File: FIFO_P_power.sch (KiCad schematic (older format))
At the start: 19 parts, among them J4 Jack-DC, U11 LM2940CT-5.0, U12 UA79M05CKCS_-5V, U13 LM2940CT-3.3

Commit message: Fix arduino header, started laying out connectors
The pins used were changed, so the old code must be rewritten to use the new pins and port D instead of port A.
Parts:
- renumbered J4 to J5, TP5 to TP4, TP6 to TP5, TP7 to TP6, TP8 to TP7, TP9 to TP8
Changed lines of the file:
@@
 $EndComp
 $Comp
-L power:GND #PWR036
+L power:GND #PWR038
 U 1 1 5C531288
 P 2950 1400
-F 0 "#PWR036" H 2950 1150 50  0001 C CNN
+F 0 "#PWR038" H 2950 1150 50  0001 C CNN
 F 1 "GND" H 2950 1250 50  0000 C CNN
 F 2 "" H 2950 1400 50  0000 C CNN
@@
 	2800 2350 2800 2600
 $Comp
-L power:GND #PWR035
+L power:GND #PWR037
 U 1 1 5C5322F0
 P 1800 2050
-F 0 "#PWR035" H 1800 1800 50  0001 C CNN
+F 0 "#PWR037" H 1800 1800 50  0001 C CNN
 F 1 "GND" H 1800 1900 50  0000 C CNN
 F 2 "" H 1800 2050 50  0000 C CNN
@@
 Connection ~ 3050 850
 $Comp
-L Connector:TestPoint TP5
+L Connector:TestPoint TP4
 U 1 1 5D244D32
 P 1400 850
-F 0 "TP5" H 1458 968 50  0000 L CNN
+F 0 "TP4" H 1458 968 50  0000 L CNN
 F 1 "TestPoint" H 1458 877 50  0000 L CNN
 F 2 "FIFO_P:Test_Pin" H 1600 850 50  0001 C CNN
@@
 $EndComp
 $Comp
-L Connector:TestPoint TP7
+L Connector:TestPoint TP6
 U 1 1 5D2450B6
 P 3050 850
-F 0 "TP7" H 3108 968 50  0000 L CNN
+F 0 "TP6" H 3108 968 50  0000 L CNN
 F 1 "TestPoint" H 3108 877 50  0000 L CNN
 F 2 "FIFO_P:Test_Pin" H 3250 850 50  0001 C CNN
@@
 $EndComp
 $Comp
-L Connector:TestPoint TP9
+L Connector:TestPoint TP8
 U 1 1 5D2454BF
 P 4600 850
-F 0 "TP9" H 4658 968 50  0000 L CNN
+F 0 "TP8" H 4658 968 50  0000 L CNN
 F 1 "TestPoint" H 4658 877 50  0000 L CNN
 F 2 "FIFO_P:Test_Pin" H 4800 850 50  0001 C CNN
@@
 $EndComp
 $Comp
-L Connector:TestPoint TP8
+L Connector:TestPoint TP7
 U 1 1 5D245994
 P 3600 2050
-F 0 "TP8" H 3658 2168 50  0000 L CNN
+F 0 "TP7" H 3658 2168 50  0000 L CNN
 F 1 "TestPoint" H 3658 2077 50  0000 L CNN
 F 2 "FIFO_P:Test_Pin" H 3800 2050 50  0001 C CNN
@@
 $EndComp
 $Comp
-L Connector:TestPoint TP6
+L Connector:TestPoint TP5
 U 1 1 5D245F67
 P 2800 2700
-F 0 "TP6" H 2650 2750 50  0000 C CNN
+F 0 "TP5" H 2650 2750 50  0000 C CNN
 F 1 "TestPoint" H 2550 2850 50  0000 C CNN
 F 2 "FIFO_P:Test_Pin" H 3000 2700 50  0001 C CNN
@@
 	3050 850  3250 850
 $Comp
-L Connector:Jack-DC J4
+L Connector:Jack-DC J5
 U 1 1 5D418214
 P 700 950
-F 0 "J4" H 700 1250 50  0000 C CNN
+F 0 "J5" H 700 1250 50  0000 C CNN
 F 1 "Jack-DC" H 700 1150 50  0000 C CNN
 F 2 "Connector_BarrelJack:BarrelJack_Horizontal" H 750 910 50  0001 C CNN
@@
 $EndComp
 $Comp
-L power:GND #PWR0101
+L power:GND #PWR036
 U 1 1 5D419D2C
 P 1150 1050
-F 0 "#PWR0101" H 1150 800 50  0001 C CNN
+F 0 "#PWR036" H 1150 800 50  0001 C CNN
 F 1 "GND" H 1155 877 50  0000 C CNN
 F 2 "" H 1150 1050 50  0001 C CNN

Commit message: Most routing done
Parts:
- added C? (x4): C, symbol Device:C
- added U?: LM2776, Package_TO_SOT_SMD:SOT-23-6, symbol Regulator_SwitchedCapacitor:LM2776
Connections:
- wire segments 37 -> 47
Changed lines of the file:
@@
 Wire Wire Line
 	2800 2700 2800 2600
+$Comp
+L Device:C C?
+U 1 1 5D14A942
+P 2100 4050
+F 0 "C?" H 2215 4096 50  0000 L CNN
+F 1 "C" H 2215 4005 50  0000 L CNN
+F 2 "" H 2138 3900 50  0001 C CNN
+F 3 "~" H 2100 4050 50  0001 C CNN
+	1    2100 4050
+	1    0    0    -1
+$EndComp
+Wire Wire Line
+	2400 3900 2100 3900
+Wire Wire Line
+	2100 4200 2350 4200
+Wire Wire Line
+	2350 4200 2350 4100
+Wire Wire Line
+	2350 4100 2400 4100
+$Comp
+L power:GND #PWR?
+U 1 1 5D14C1B1
+P 2800 4300
+F 0 "#PWR?" H 2800 4050 50  0001 C CNN
+F 1 "GND" H 2805 4127 50  0000 C CNN
+F 2 "" H 2800 4300 50  0001 C CNN
+F 3 "" H 2800 4300 50  0001 C CNN
+	1    2800 4300
+	1    0    0    -1
+$EndComp
+$Comp
+L Regulator_SwitchedCapacitor:LM2776 U?
+U 1 1 5D148E12
+P 2800 3900
+F 0 "U?" H 3150 3900 50  0000 L CNN
+F 1 "LM2776" H 3150 3800 50  0000 L CNN
+F 2 "Package_TO_SOT_SMD:SOT-23-6" H 2850 3550 50  0001 L CNN
+F 3 "http://www.ti.com/lit/ds/symlink/lm2776.pdf" H 950 5150 50  0001 C CNN
+	1    2800 3900
+	1    0    0    -1
+$EndComp
+Wire Wire Line
+	2400 3800 2350 3800
+Wire Wire Line
+	2350 3800 2350 3550
+Wire Wire Line
+	2350 3550 2800 3550
+Wire Wire Line
+	2800 3550 2800 3600
+Wire Wire Line
+	3200 3800 3650 3800
+$Comp
+L Device:C C?
+U 1 1 5D150015
+P 3650 3950
+F 0 "C?" H 3765 3996 50  0000 L CNN
+F 1 "C" H 3765 3905 50  0000 L CNN
+F 2 "" H 3688 3800 50  0001 C CNN
+F 3 "~" H 3650 3950 50  0001 C CNN
+	1    3650 3950
+	1    0    0    -1
+$EndComp
+Connection ~ 3650 3800
+Wire Wire Line
+	3650 3800 4000 3800
+$Comp
+L Device:C C?
+U 1 1 5D15083E
+P 4000 3950
+F 0 "C?" H 4115 3996 50  0000 L CNN
+F 1 "C" H 4115 3905 50  0000 L CNN
+F 2 "" H 4038 3800 50  0001 C CNN
+F 3 "~" H 4000 3950 50  0001 C CNN
+	1    4000 3950
+	1    0    0    -1
+$EndComp
+$Comp
+L power:GND #PWR?
+U 1 1 5D150EB8
+P 3650 4100
+F 0 "#PWR?" H 3650 3850 50  0001 C CNN
+F 1 "GND" H 3655 3927 50  0000 C CNN
+F 2 "" H 3650 4100 50  0001 C CNN
+F 3 "" H 3650 4100 50  0001 C CNN
+	1    3650 4100
+	1    0    0    -1
+$EndComp
+$Comp
+L power:GND #PWR?
+U 1 1 5D15173D
+P 4000 4100
+F 0 "#PWR?" H 4000 3850 50  0001 C CNN
+F 1 "GND" H 4005 3927 50  0000 C CNN
+F 2 "" H 4000 4100 50  0001 C CNN
+F 3 "" H 4000 4100 50  0001 C CNN
+	1    4000 4100
+	1    0    0    -1
+$EndComp
+$Comp
+L Device:C C?
+U 1 1 5D151B07
+P 2950 3550
+F 0 "C?" V 2698 3550 50  0000 C CNN
+F 1 "C" V 2789 3550 50  0000 C CNN
+F 2 "" H 2988 3400 50  0001 C CNN
+F 3 "~" H 2950 3550 50  0001 C CNN
+	1    2950 3550
+	0    1    1    0
+$EndComp
+Connection ~ 2800 3550
+$Comp
+L power:GND #PWR?
+U 1 1 5D152ECC
+P 3100 3550
+F 0 "#PWR?" H 3100 3300 50  0001 C CNN
+F 1 "GND" V 3105 3422 50  0000 R CNN
+F 2 "" H 3100 3550 50  0001 C CNN
+F 3 "" H 3100 3550 50  0001 C CNN
+	1    3100 3550
+	0    -1   -1   0
+$EndComp
 $EndSCHEMATC

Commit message: Added inverter for -5V
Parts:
- removed C22, C26: 22uF, Capacitor_THT:C_Disc_D5.0mm_W2.5mm_P2.50mm, symbol Device:C
- removed C23, C27: .47uF, Capacitor_THT:C_Disc_D5.0mm_W2.5mm_P2.50mm, symbol Device:C
- removed C?: C, symbol Device:C
- removed TP5, TP7: TestPoint, FIFO_P:Test_Pin, symbol Connector:TestPoint
- removed U12: UA79M05CKCS_-5V, Package_TO_SOT_THT:TO-220-3_Vertical, symbol FIFO_P:UA79M05CKCS_-5V
- added C31: 22uF, Capacitor_THT:C_Disc_D5.0mm_W2.5mm_P2.50mm, symbol Device:C
- added TP6: TestPoint, FIFO_P:Test_Pin, symbol Connector:TestPoint
- C20, C25: renamed from C?; value C -> .47uF; footprint (none) -> Capacitor_THT:C_Disc_D5.0mm_W2.5mm_P2.50mm
- C27: renamed from C?; value C -> 22uF; footprint (none) -> Capacitor_THT:C_Disc_D5.0mm_W2.5mm_P2.50mm
- gave numbers to parts that had none: 1
- renumbered C20 to C21, C21 to C22, C24 to C26, C25 to C28, C28 to C29, C29 to C30, TP6 to TP5, TP8 to TP7, U11 to U12
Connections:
- wire segments 47 -> 36
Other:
- note added: "A low-noise power supply can improve the accuracy and stability of the circuit. \nThis page includes a possible implementation. Using the suggested chips:\n\nVin+ = 7 to 25V"
- note removed: "A low-noise power supply can improve the accuracy and stability of the circuit. \nThis page includes a possible implementation. Using the Suggested chips:\n\nVin+ = 7 to 25V\nVin- = -7 to -25V"
- moved on the sheet: C20, C25, C27, U11

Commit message: Partial jumpers
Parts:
- U12, U13: footprint Package_TO_SOT_THT:TO-220-3_Vertical -> Package_TO_SOT_THT:TO-220-3_Horizontal_TabDown
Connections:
- wire segments 36 -> 35
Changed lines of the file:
@@
 F 0 "U12" H 1950 1100 50  0000 C CNN
 F 1 "LM2940CT-5.0" H 2150 1100 50  0000 L CNN
-F 2 "Package_TO_SOT_THT:TO-220-3_Vertical" H 2150 1200 50  0000 C CIN
+F 2 "Package_TO_SOT_THT:TO-220-3_Horizontal_TabDown" H 2150 1200 50  0000 C CIN
 F 3 "" H 2150 900 50  0000 C CNN
 	1    2150 900
@@
 F 0 "U13" H 3600 1100 50  0000 C CNN
 F 1 "LM2940CT-3.3" H 3800 1100 50  0000 L CNN
-F 2 "Package_TO_SOT_THT:TO-220-3_Vertical" H 3800 1200 50  0000 C CIN
+F 2 "Package_TO_SOT_THT:TO-220-3_Horizontal_TabDown" H 3800 1200 50  0000 C CIN
 F 3 "" H 3800 900 50  0000 C CNN
 	1    3800 900
@@
 	1    0    0    -1
 $EndComp
-Connection ~ 1650 2000
-Wire Wire Line
-	1700 2000 1650 2000
-$Comp
-L power:GND #PWR038
-U 1 1 5D152ECC
-P 1700 2000
-F 0 "#PWR038" H 1700 1750 50  0001 C CNN
-F 1 "GND" V 1705 1872 50  0000 R CNN
-F 2 "" H 1700 2000 50  0001 C CNN
-F 3 "" H 1700 2000 50  0001 C CNN
-	1    1700 2000
-	0    -1   -1   0
-$EndComp
-$Comp
+$Comp

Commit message: Begin cleaning up schematic. FIFO-DAC area ripped up
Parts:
- removed U13: LM2940CT-3.3, Package_TO_SOT_THT:TO-220-3_Horizontal_TabDown, symbol FIFO_P:LM2940CT-3.3
- added U7: LM1117-3.3, Package_TO_SOT_SMD:TO-252-3_TabPin2, symbol Regulator_Linear:LM1117-3.3
- C20, C22, C25, C28, C30: value .47uF -> 470n
- C21, C26, C27, C29, C31: value 22uF -> 22u
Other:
- note added: "A low-noise power supply can improve the accuracy and stability of the circuit. \nThis page includes a possible implementation. Using the suggested chips:\n\nVin+ = 6 to 25V"
- note removed: "A low-noise power supply can improve the accuracy and stability of the circuit. \nThis page includes a possible implementation. Using the suggested chips:\n\nVin+ = 7 to 25V"
- moved on the sheet: C20, C25, C27, C31, TP6, U11

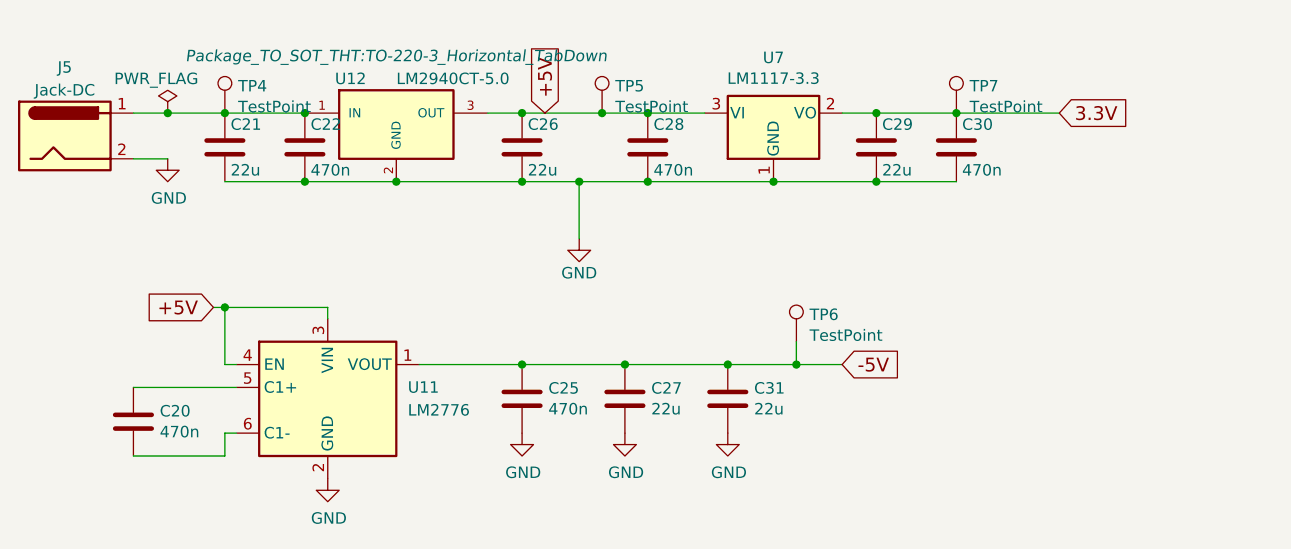
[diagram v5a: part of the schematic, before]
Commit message: Added screw terminal; put some new IC footprints in place
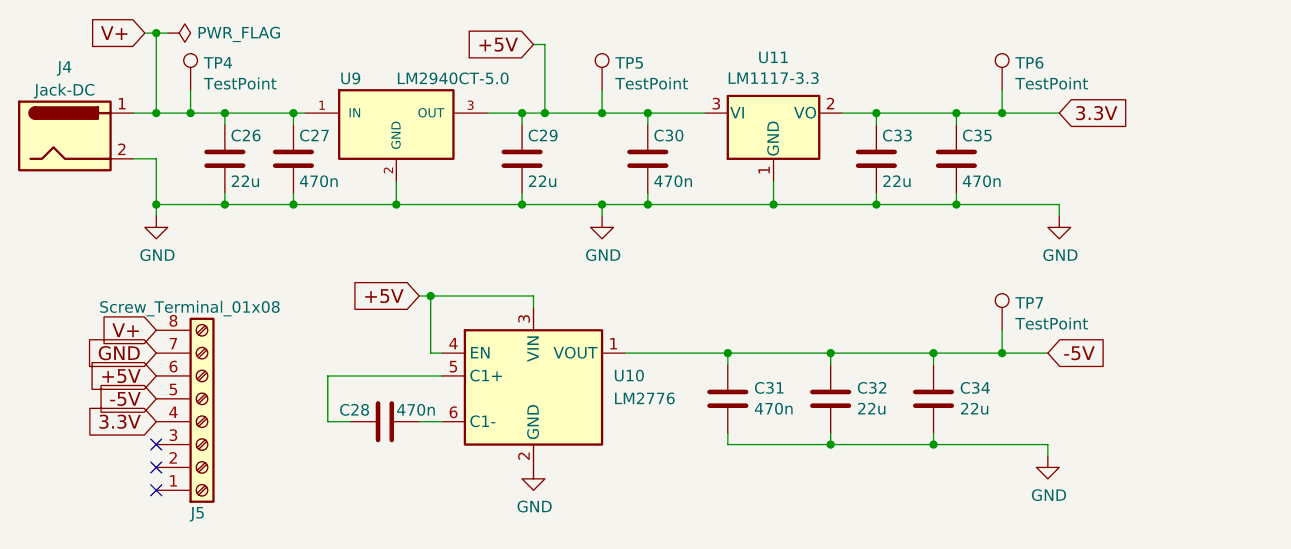
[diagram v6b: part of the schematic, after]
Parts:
- added J5: Screw_Terminal_01x08, TerminalBlock_Phoenix:TerminalBlock_Phoenix_MKDS-3-8-5.08_1x08_P5.08mm_Horizontal, symbol Connector:Screw_Terminal_01x08
- renumbered C21 to C26, C22 to C27, C20 to C28, C26 to C29, C28 to C30, C25 to C31, C27 to C32, C29 to C33, C31 to C34, C30 to C35, J5 to J4, TP7 to TP6, TP6 to TP7, U11 to U10, U7 to U11, U12 to U9
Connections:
- net +5V: now also J5.6 (Pin_6)
- net -5V: now also J5.5 (Pin_5)
- net 3.3V: now also J5.4 (Pin_4)
- net GND: now also J5.7 (Pin_7)
- net V+: now reaches C26.1, C27.1, J4.1, TP4.1, U9.1 (IN)
- net V+: now also J5.8 (Pin_8)
- net at U10.5 (C1+): now also C28.2; no longer C28.1
- net at U10.6 (C1-): now also C28.1; no longer C28.2
- no-connect marks 0 -> 3
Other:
- moved on the sheet: C26, C27, C28, C29, C30, C31, C32, C33, C34, C35, TP4, TP5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

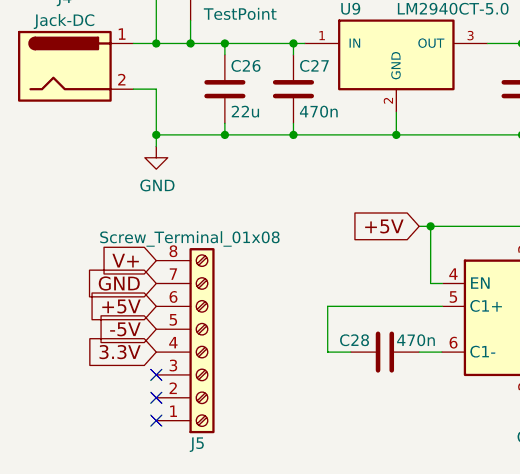
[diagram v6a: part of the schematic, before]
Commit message: Flipped Due pins to be correct to actual
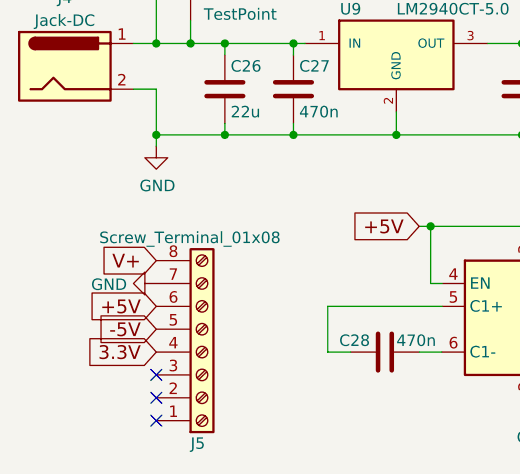
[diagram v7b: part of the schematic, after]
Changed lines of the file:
@@
 Text GLabel 1100 1800 0    60   Input ~ 0
 V+
-Text GLabel 1100 1900 0    60   Input ~ 0
-GND
 Text GLabel 1100 2000 0    60   Input ~ 0
 +5V
@@
 Wire Wire Line
 	1850 2000 2350 2000
+$Comp
+L power:GND #PWR0101
+U 1 1 5D5F232E
+P 1100 1900
+F 0 "#PWR0101" H 1100 1650 50  0001 C CNN
+F 1 "GND" V 1105 1772 50  0000 R CNN
+F 2 "" H 1100 1900 50  0001 C CNN
+F 3 "" H 1100 1900 50  0001 C CNN
+	1    1100 1900
+	0    1    1    0
+$EndComp
 $EndSCHEMATC

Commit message: More progress on final board
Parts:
- added C28, C35: 1u, Capacitor_SMD:C_0805_2012Metric_Pad1.15x1.40mm_HandSolder, symbol Device:C
- added C31: 10u, Capacitor_SMD:C_0805_2012Metric_Pad1.15x1.40mm_HandSolder, symbol Device:C
- C26: value 22u -> 10u; footprint Capacitor_THT:C_Disc_D5.0mm_W2.5mm_P2.50mm -> Capacitor_SMD:C_0805_2012Metric_Pad1.15x1.40mm_HandSolder
- C27: value 470n -> 10u; footprint Capacitor_THT:C_Disc_D5.0mm_W2.5mm_P2.50mm -> Capacitor_SMD:C_0805_2012Metric_Pad1.15x1.40mm_HandSolder
- C29: renamed from C28; value 470n -> 1u; footprint Capacitor_THT:C_Disc_D5.0mm_W2.5mm_P2.50mm -> Capacitor_SMD:C_0805_2012Metric_Pad1.15x1.40mm_HandSolder
- C30: renamed from C29; value 22u -> 10u; footprint Capacitor_THT:C_Disc_D5.0mm_W2.5mm_P2.50mm -> Capacitor_SMD:C_0805_2012Metric_Pad1.15x1.40mm_HandSolder
- C32: renamed from C30; value 470n -> 1u; footprint Capacitor_THT:C_Disc_D5.0mm_W2.5mm_P2.50mm -> Capacitor_SMD:C_0805_2012Metric_Pad1.15x1.40mm_HandSolder
- C33: renamed from C31; value 470n -> 1u; footprint Capacitor_THT:C_Disc_D5.0mm_W2.5mm_P2.50mm -> Capacitor_SMD:C_0805_2012Metric_Pad1.15x1.40mm_HandSolder
- C34: renamed from C32; value 22u -> 10u; footprint Capacitor_THT:C_Disc_D5.0mm_W2.5mm_P2.50mm -> Capacitor_SMD:C_0805_2012Metric_Pad1.15x1.40mm_HandSolder
- C36: renamed from C35; value 470n -> 10u; footprint Capacitor_THT:C_Disc_D5.0mm_W2.5mm_P2.50mm -> Capacitor_SMD:C_0805_2012Metric_Pad1.15x1.40mm_HandSolder
- C37: renamed from C34; value 22u -> 10u; footprint Capacitor_THT:C_Disc_D5.0mm_W2.5mm_P2.50mm -> Capacitor_SMD:C_0805_2012Metric_Pad1.15x1.40mm_HandSolder
- C38: renamed from C33; value 22u -> 10u; footprint Capacitor_THT:C_Disc_D5.0mm_W2.5mm_P2.50mm -> Capacitor_SMD:C_0805_2012Metric_Pad1.15x1.40mm_HandSolder
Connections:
- net +5V: now also C31.1
- net 3.3V: now also C35.1
- net GND: now also C28.2, C31.2, C35.2
- net V+: now also C28.1
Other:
- moved on the sheet: C26, C27, C32, C36, C38
